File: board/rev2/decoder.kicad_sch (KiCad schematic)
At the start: 12 parts, among them U10 IS61LV256AL, U11 74AHCT595, U2 74VHC163, U9 74VHC163

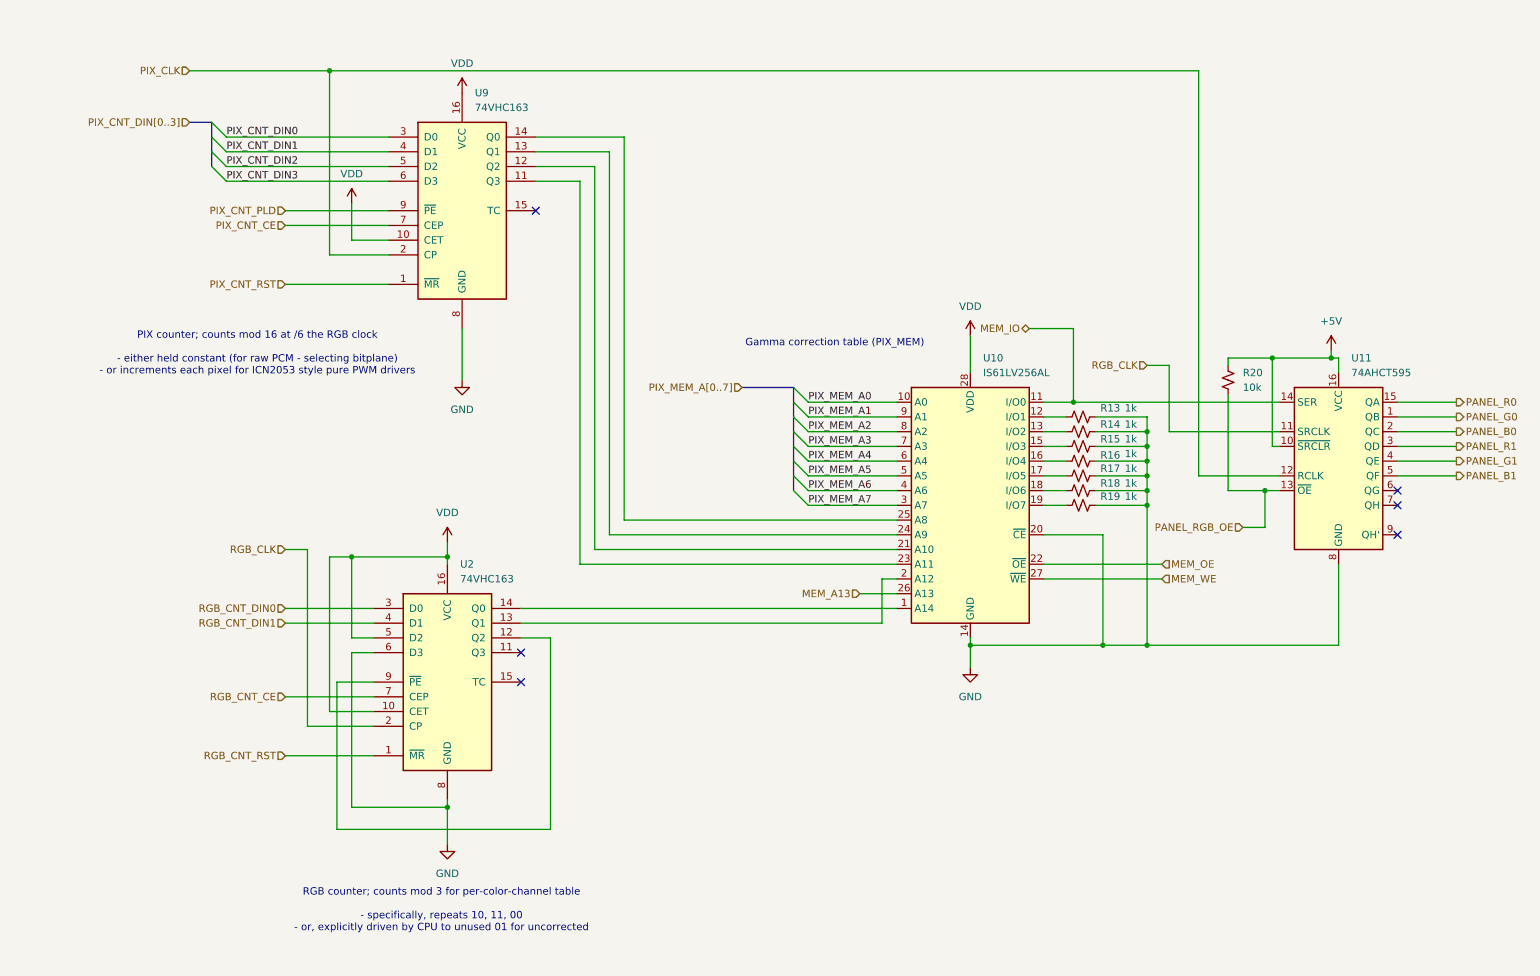
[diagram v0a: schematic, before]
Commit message: Continue board work
- move to rp2040, separate stm32g071 to do usb-c + aux ctrl IO
  - still cheaper lol with the cost of stm32s
- more power reg stuff
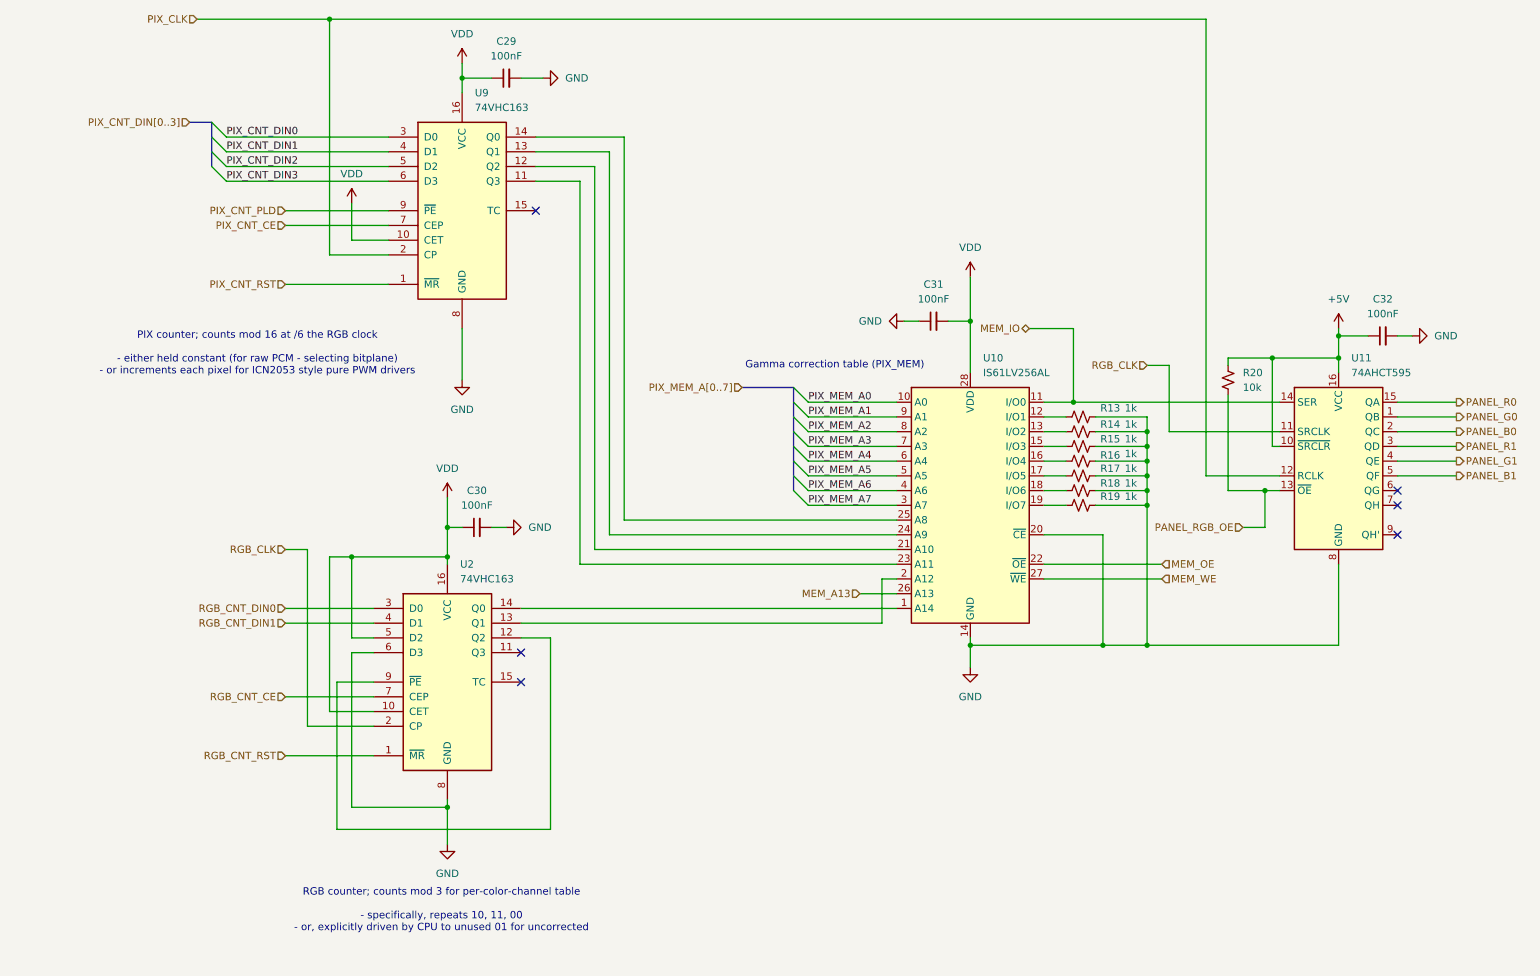
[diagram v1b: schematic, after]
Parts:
- added C29, C30, C31, C32: 100nF, symbol Device:C_Small
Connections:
- net +5V: now also C32.1
- net GND: now also C29.2, C30.2, C31.1, C32.2
- net VDD: now also C29.1, C30.1, C31.2

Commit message: Split out board into A/B
allow 2x displays (for chaining)
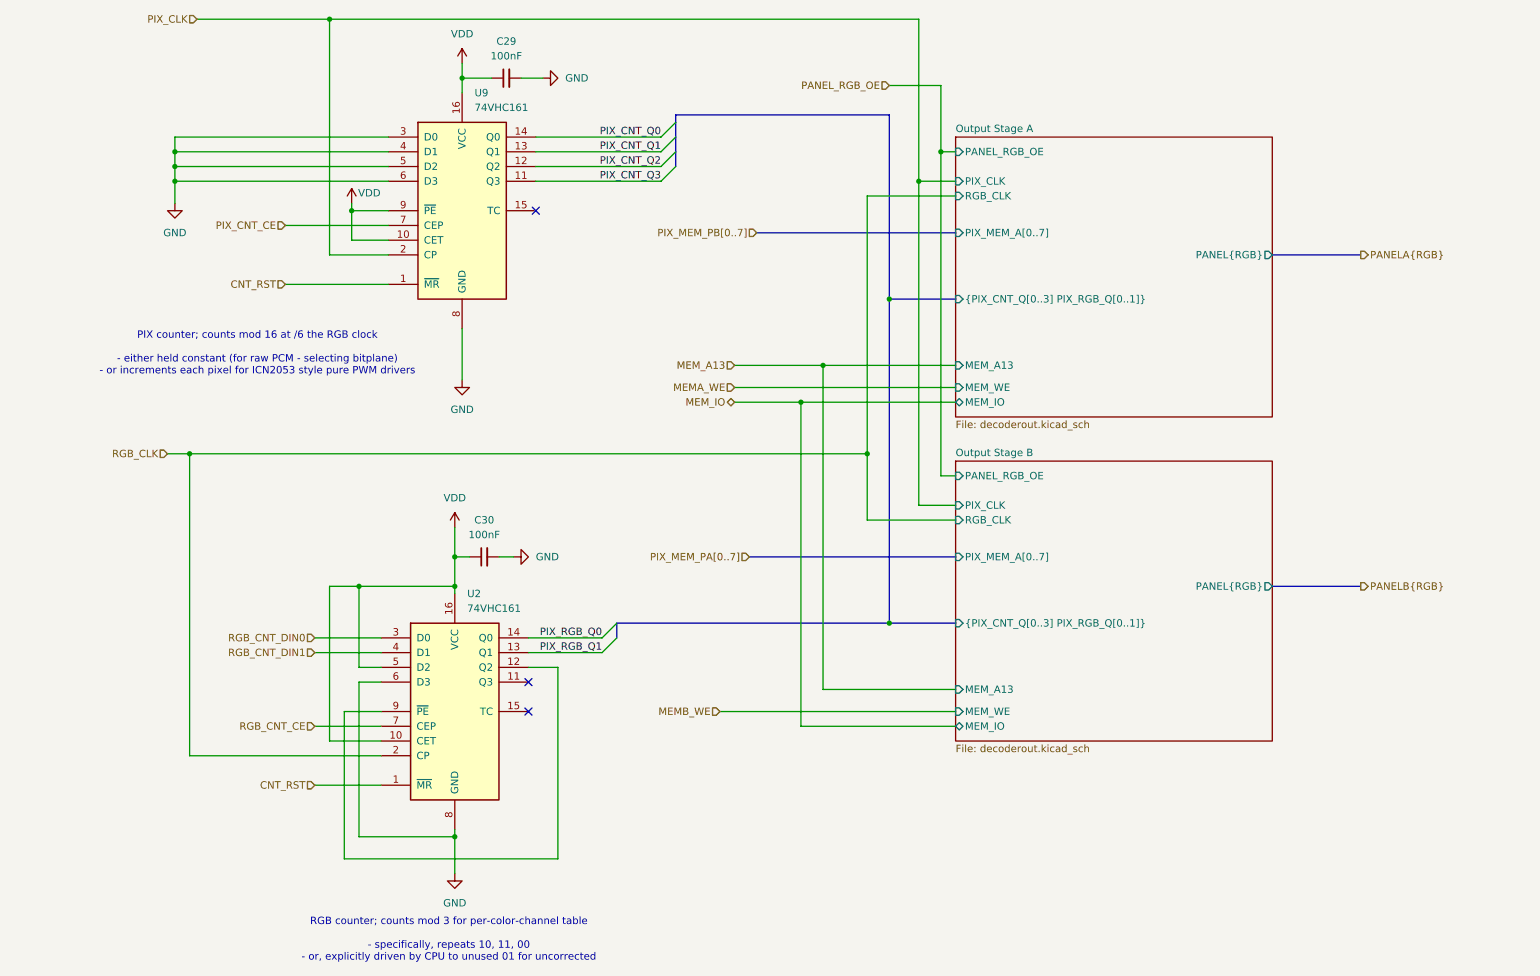
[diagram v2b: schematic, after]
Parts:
- removed C31, C32: 100nF, symbol Device:C_Small
- removed R13, R14, R15, R16, R17, R18, R19: 1k, symbol Device:R_Small_US
- removed R20: 10k, symbol Device:R_Small_US
- removed U10: IS61LV256AL, Package_SO:SOP-28_8.4x18.16mm_P1.27mm, symbol Memory_RAM:IS62C256AL
- removed U11: 74AHCT595, symbol 74xx:74AHCT595
- U2, U9: value 74VHC163 -> 74VHC161
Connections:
- net PIX_CNT_DIN0 is gone; now on net GND: U9.3 (D0)
- net PIX_CNT_DIN1 is gone; now on net GND: U9.4 (D1)
- net PIX_CNT_DIN2 is gone; now on net GND: U9.5 (D2)
- net PIX_CNT_DIN3 is gone; now on net GND: U9.6 (D3)
- net PIX_CNT_PLD is gone; now on net VDD: U9.9 (~{PE})
- net RGB_CNT_RST is gone; now on net CNT_RST: U2.1 (~{MR})
- net PIX_RGB_Q0: now reaches U2.14 (Q0)
- net PIX_RGB_Q1: now reaches U2.13 (Q1)
- net PIX_CNT_Q2: now reaches U9.12 (Q2)
- net PIX_CNT_Q3: now reaches U9.11 (Q3)
- net PIX_CNT_Q1: now reaches U9.13 (Q1)
- net PIX_CNT_Q0: now reaches U9.14 (Q0)
- net PIX_CNT_RST renamed CNT_RST
- no-connect marks 6 -> 3
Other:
- added sheet Output Stage A (decoderout.kicad_sch)
- added sheet Output Stage B (decoderout.kicad_sch)
- note removed: "Gamma correction table (PIX_MEM)"
- moved on the sheet: C30, U2

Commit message: More board work
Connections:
- net GND: no longer U9.3 (D0), U9.4 (D1), U9.5 (D2), U9.6 (D3)
- net VDD: no longer U9.9 (~{PE})
- new net PIX_CNT_DIN0: U9.3 (D0)
- new net PIX_CNT_DIN1: U9.4 (D1)
- new net PIX_CNT_DIN2: U9.5 (D2)
- new net PIX_CNT_DIN3: U9.6 (D3)
- new net PIX_CNT_PE: U9.9 (~{PE})

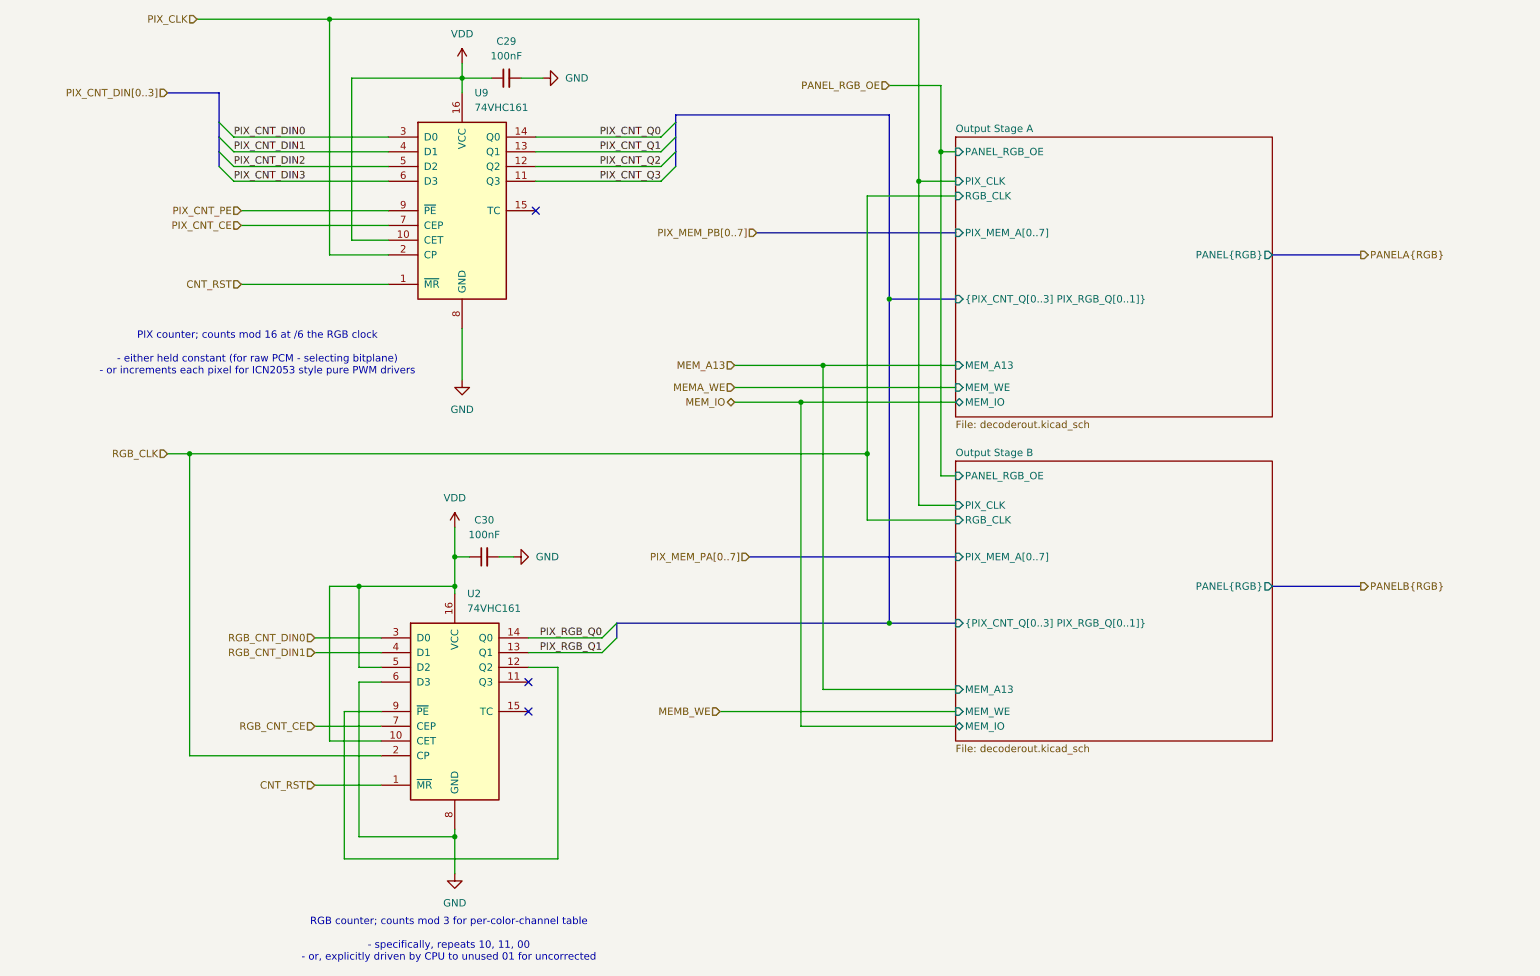
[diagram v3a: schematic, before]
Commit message: Board GPIO allocation
- and usbmux

still need to do termination on the big buses + a bunch of bypass caps
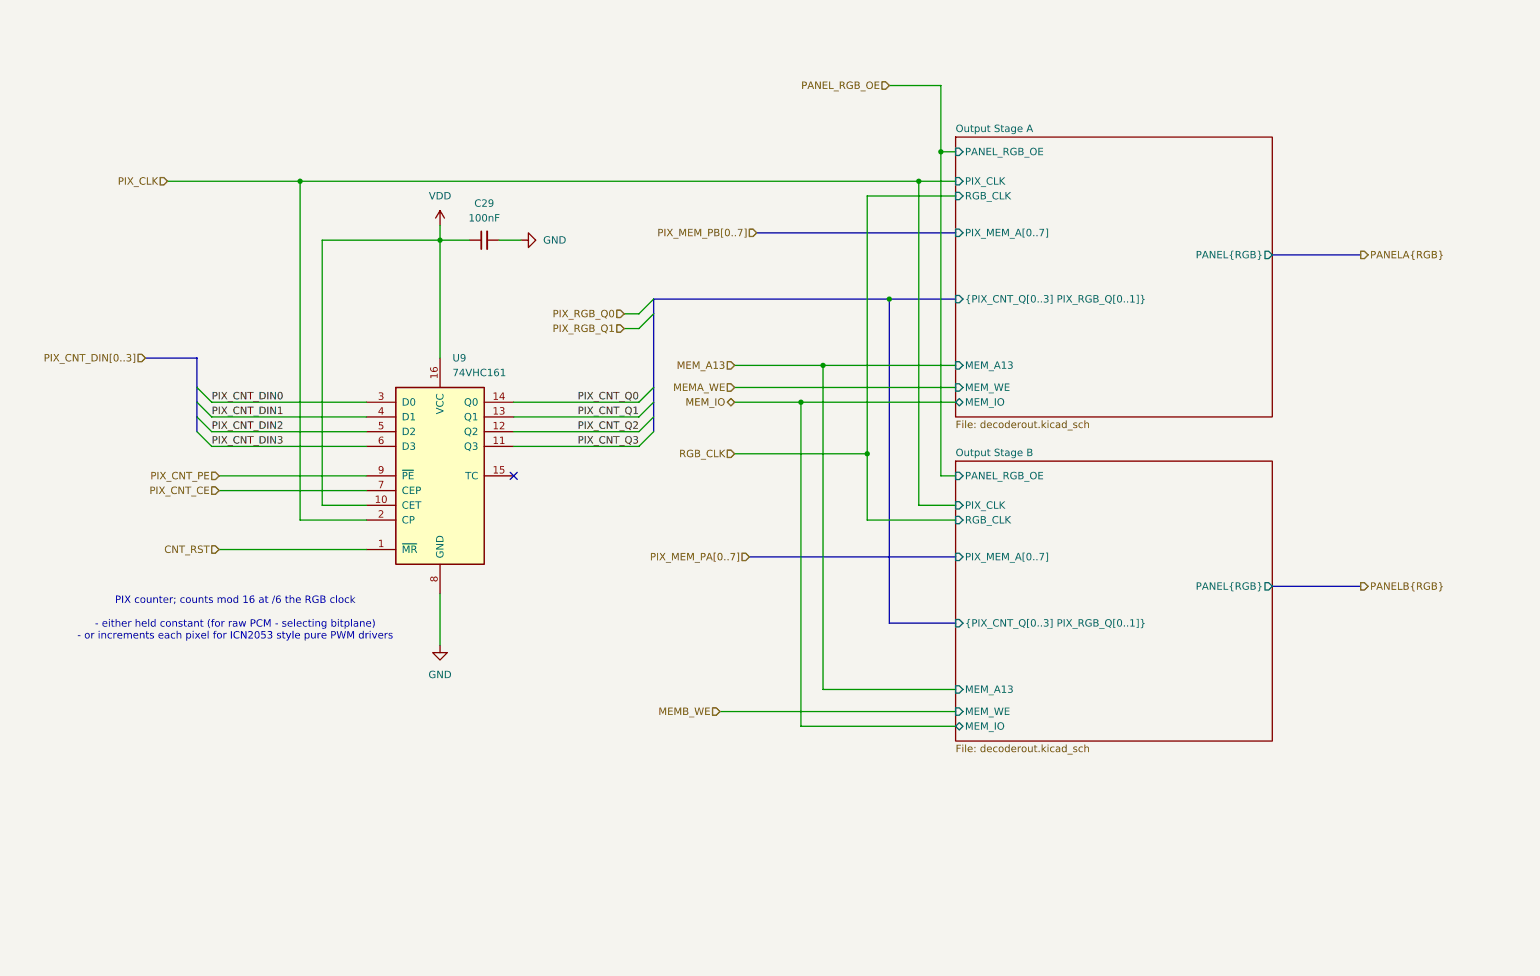
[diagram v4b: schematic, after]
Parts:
- removed C30: 100nF, symbol Device:C_Small
- removed U2: 74VHC161, symbol 74xx:74LS163
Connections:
- no-connect marks 3 -> 1
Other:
- note removed: "RGB counter; counts mod 3 for per-color-channel table - specifically, repeats 10, 11, 00 - or, explicitly driven by CPU to unused 01 for uncorrected"
- company: (none) -> MLABS
- title: (none) -> LED Bitstream Generator (common half)
- moved on the sheet: C29, U9
